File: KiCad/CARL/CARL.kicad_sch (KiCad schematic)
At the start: 46 parts, among them J1 Barrel_Jack (5V DC Supply), SW1 Beat_In_1, SW10 Power Switch, SW11 Mute_Button, SW12 Move_Left_Button, SW13 Move_Right_Button, SW14 Play_Button, SW2 Beat_In_2, SW3 Beat_In_3, SW4 Beat_In_4, SW5 Beat_In_5, SW6 Beat_In_6, SW7 Beat_In_7, SW8 Beat_In_8, SW9 Save_and_Load_Button, U1 NHD-0420H1Z (LCD), U2 MIC5365-3.3YC5 (5V to 3.3V re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, U3 MAX98357A (Amplifier), U4 TLC5947DAP (LED Driver), U5 MCP23017_SO

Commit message: PCB V2 and Schematic V3
-Updated schematic to utilize new voltage regulator setup.
-Updated PCB to reflect changes done in the schematic
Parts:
- removed U2: MIC5365-3.3YC5 (5V to 3.3V regulator), Package_TO_SOT_SMD:SOT-353_SC-70-5, symbol Regulator_Linear:MIC5365-3.3YC5
- added C10, C3, C4, C5, C6, C8, C9: 100nF, Capacitor_SMD:C_0805_2012Metric, symbol Device:C_Small
- added C7: 100nf, Capacitor_SMD:C_0805_2012Metric, symbol Device:C_Small
- added U2, U7, U9: L7805 (5V Voltage Regulator), Package_TO_SOT_THT:TO-220-3_Vertical, symbol Regulator_Linear:L7805
- added U6, U8: LD1117V33 (3.3V Voltage Regulator), Package_TO_SOT_THT:TO-220-3_Vertical, symbol Regulator_Linear:LD1117V33
- C1: value 330nF -> 100nf
- J1: value Barrel_Jack (5V DC Supply) -> Barrel_Jack (9V DC Supply)
- RV2: value Gain_Control -> Gain_Control (10k POT); footprint Potentiometer_THT:Potentiometer_Bourns_3009Y_Horizontal -> Potentiometer_SMD:Potentiometer_ACP_CA6-VSMD_Vertical
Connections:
- net GND: now also C10.2, C3.2, C4.2, C5.2, C6.2, C7.2, C8.2, C9.2, U2.2 (GND), U6.1 (GND), U7.2 (GND), U8.1 (GND), U9.2 (GND)
- net 5V -ESP32 Power: now reaches A1.26 (USB)
- net 5V -ESP32 Power: now also C4.1, U2.3 (OUT)
- net 3.3V renamed 3.3V -LCD Power
- net 3.3V -LCD Power: now also U6.2 (VO); no longer A1.2 (3V3), U5.17 (A2), U5.9 (VDD)
- net 5V renamed 5V -LED Driver Power
- net 5V -LED Driver Power: now also C10.1, U9.3 (OUT); no longer C1.1, R18.2, RV2.1, SW10.2 (B), U3.7 (VDD), U3.8 (VDD)
- new net: C1.1, C3.1, C5.1, C7.1, C9.1, SW10.2 (B), U2.1 (IN), U6.3 (VI), U7.1 (IN), U8.3 (VI), U9.1 (IN)
- new net 3.3V -GPIO Extender Power: C8.1, U5.17 (A2), U5.9 (VDD), U8.2 (VO)
- new net 5V -Amplifier Power: C6.1, R18.2, RV2.1, U3.7 (VDD), U3.8 (VDD), U7.3 (OUT)
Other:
- note added: "Power Module"
- moved on the sheet: C1, C2

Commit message: Minor Schematic Update
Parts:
- added R1, R2: 4.7Kohm, Resistor_SMD:R_0805_2012Metric, symbol Device:R_Small_US
- added R3: 0ohm, Resistor_SMD:R_0805_2012Metric, symbol Device:R_Small_US
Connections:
- net at U3.1 (DIN): now also A1.5 (DAC2/A0); no longer A1.7 (I34/A2)
- net at U3.14 (LRCLK): now also A1.11 (SCK/IO5); no longer A1.9 (IO36/A4)
- net at U3.16 (BCLK): now also A1.6 (DAC1/A1); no longer A1.8 (I39/A3)
- net at A1.10 (IO4/A5): now also U4.3 (SCLK)
- net at U1.4 (RS): now also A1.13 (MISO/IO19); no longer A1.11 (SCK/IO5)
- net at A1.14 (RX/IO16): now also R3.1; no longer U4.29 (SOUT)
- net at A1.17 (SDA/IO23), U5.13 (SDA): now also R1.2
- net at A1.18 (SCL/IO22), U5.12 (SCK): now also R2.2; no longer U4.3 (SCLK)
- new net: R3.2, U4.29 (SOUT)
- no-connect marks 23 -> 22
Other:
- note added: "Multiple of same voltage regulators to reduce heat produced by the regulators."
- note removed: "Says SCK (SPI clock) but chip uses I2C (SLC). Odd pin labeling or error on our part?"

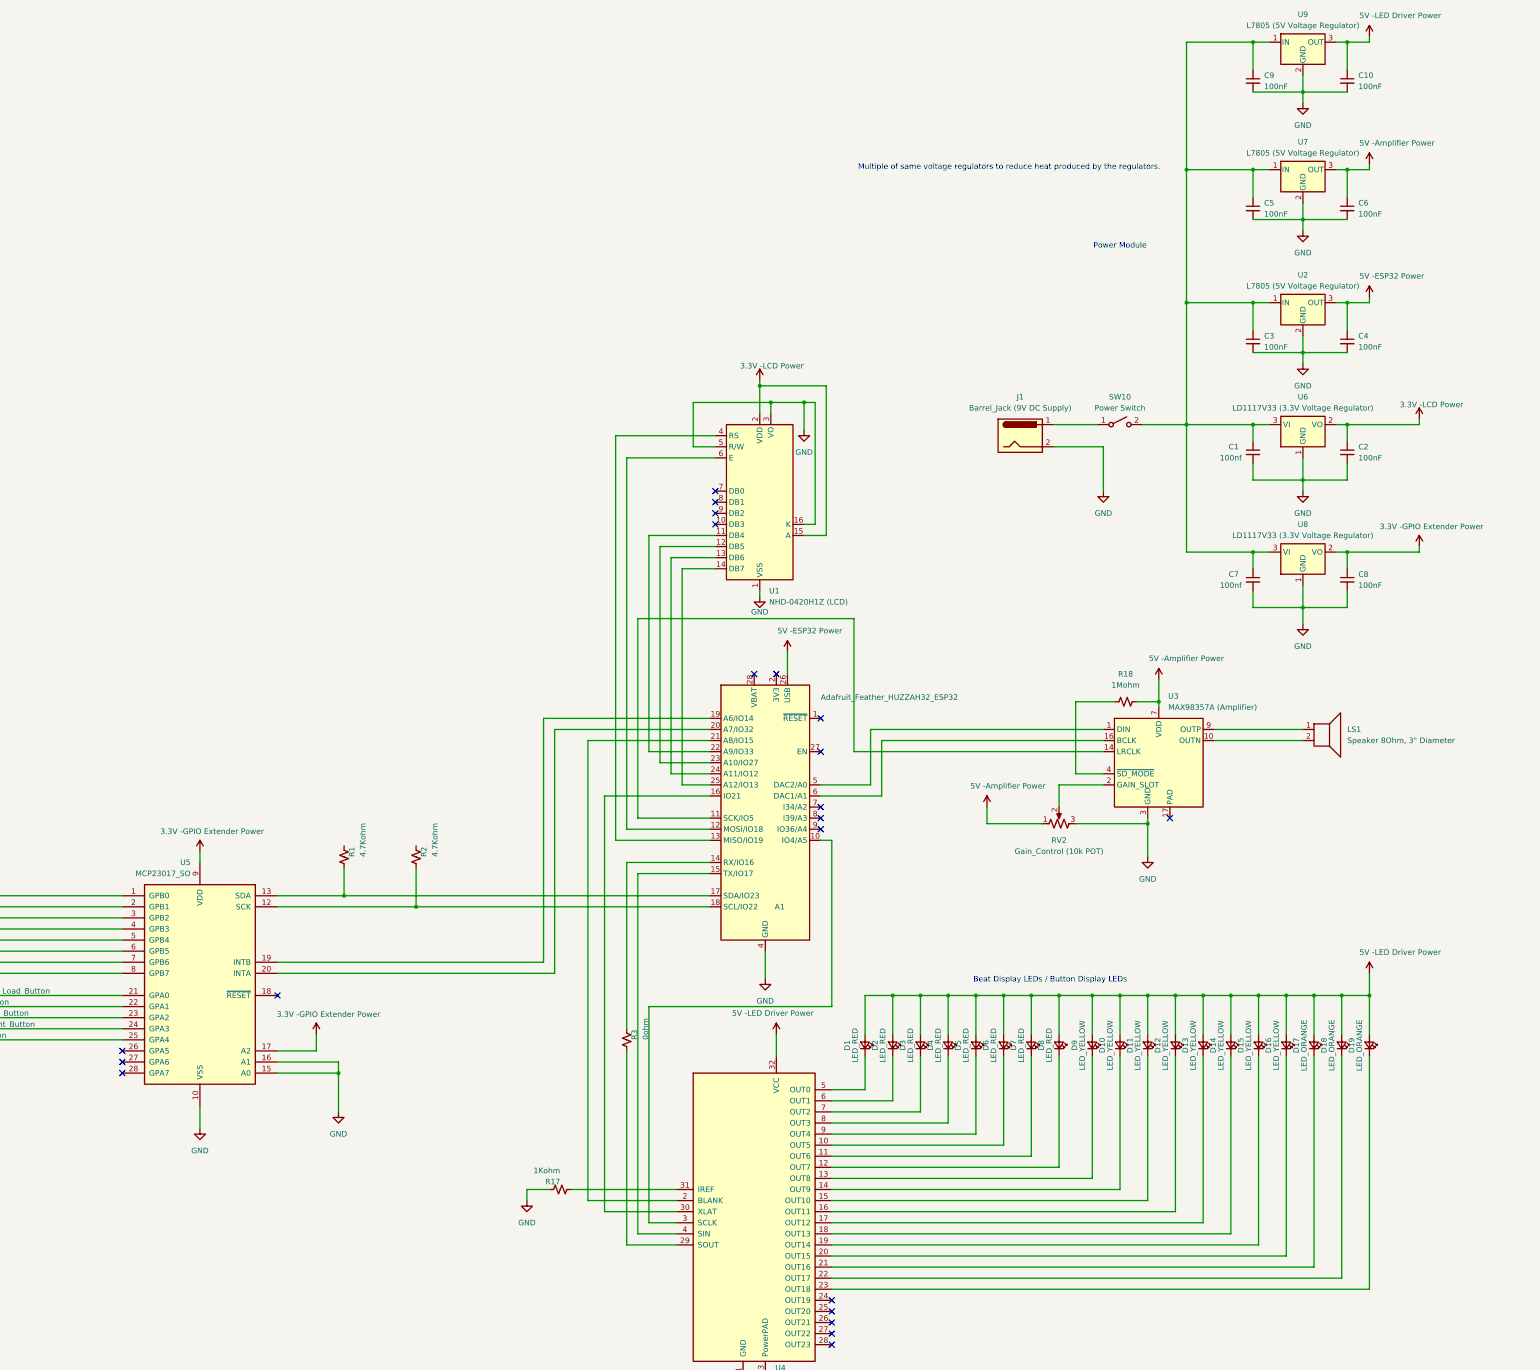
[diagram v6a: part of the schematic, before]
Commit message: Final Schematic and PCB
-Added test points  and 0 ohm resistors to the schematic.
-Added pullup resistors to I2C line
-Updated PCB and redid layout according to updated schematic.
-LED footprint updated to typical through hole PCB.
-Generated Gerbur Files
-Added Mounting Holes and Silkscreen
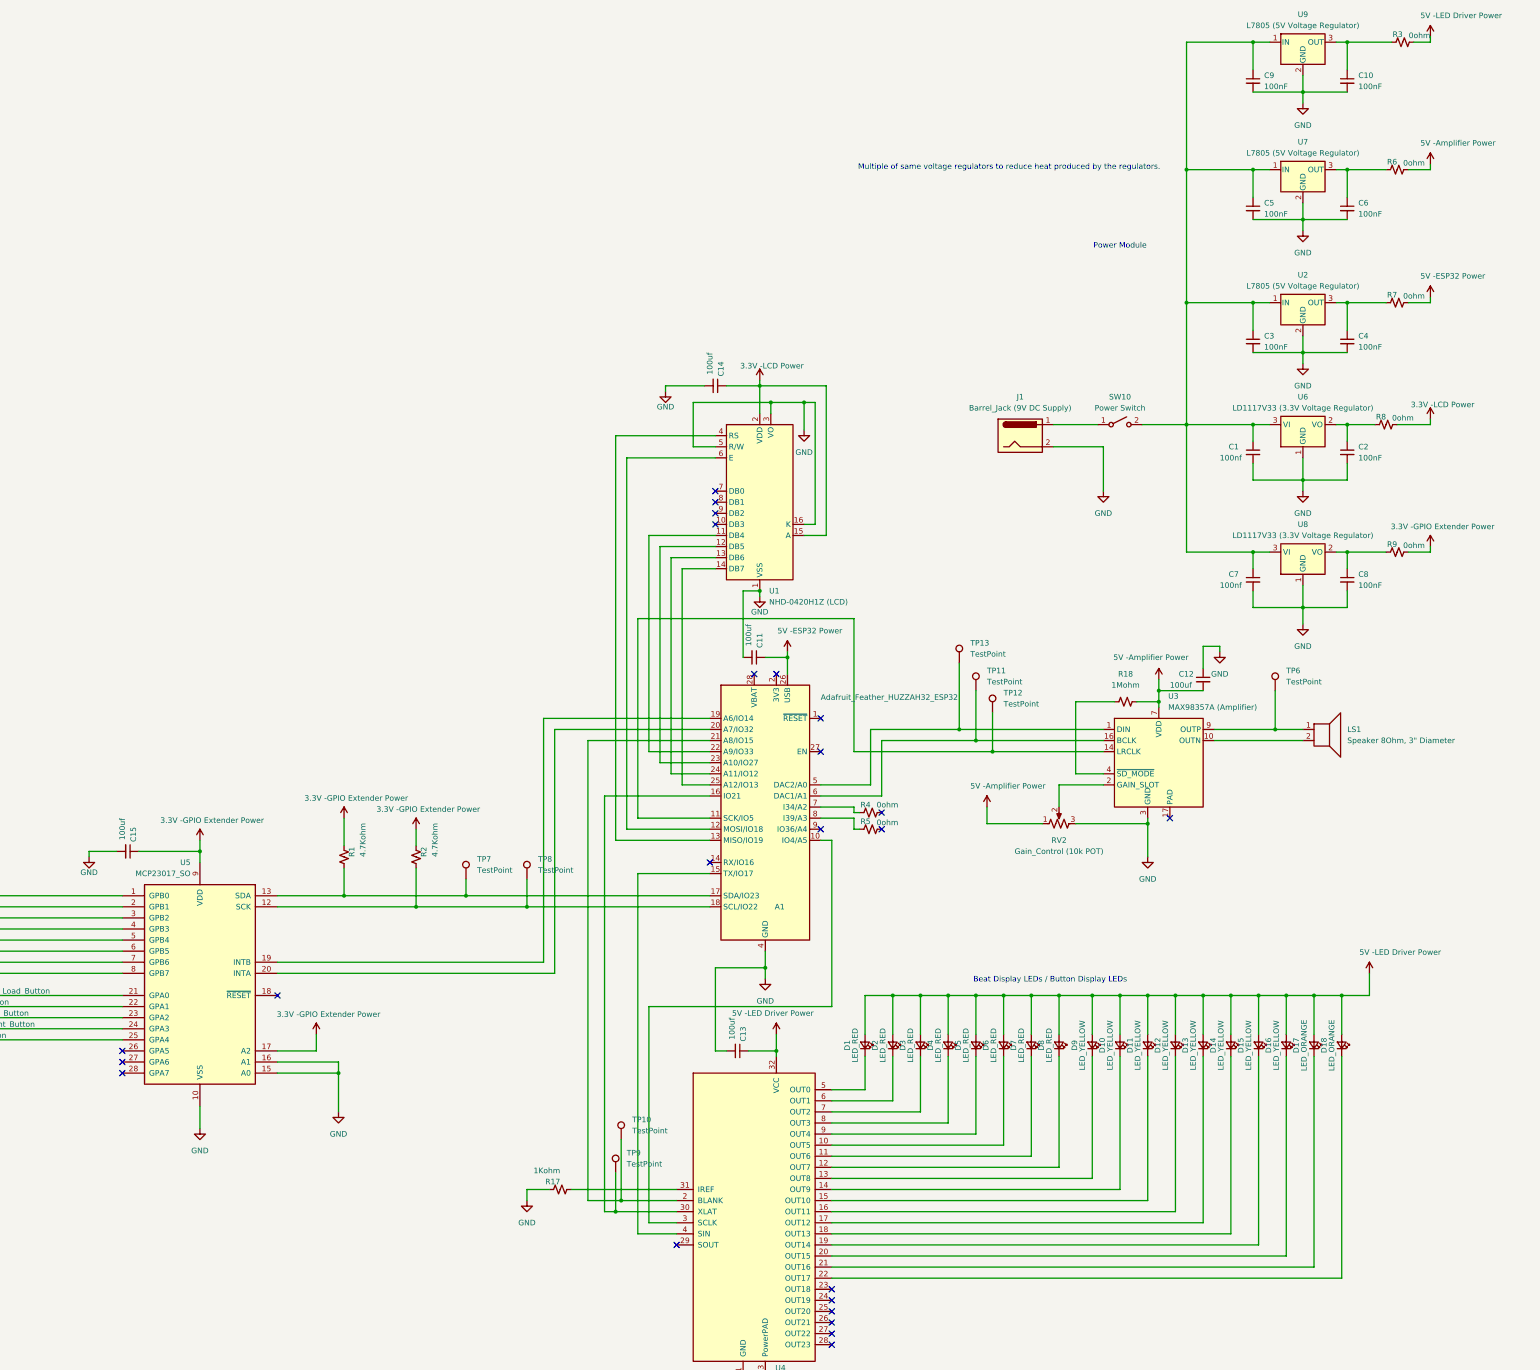
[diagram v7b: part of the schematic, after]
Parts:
- removed D19: LED_ORANGE, LED_SMD:LED_0805_2012Metric, symbol Device:LED_Small
- added C11, C12, C13, C14, C15: 100uf, Capacitor_SMD:C_0805_2012Metric, symbol Device:C_Small
- added R4, R5, R6, R7, R8, R9: 0ohm, Connector_PinHeader_2.54mm:PinHeader_1x02_P2.54mm_Vertical, symbol Device:R_Small_US
- added TP10, TP11, TP12, TP13, TP6, TP7, TP8, TP9: TestPoint, Connector_PinHeader_2.54mm:PinHeader_1x01_P2.54mm_Vertical, symbol Connector:TestPoint
- D1, D10, D11, D12, D13, D14, D15, D16, D17, D18, D2, D3, D4, D5, D6, D7, D8, D9: footprint LED_SMD:LED_0805_2012Metric -> LED_THT:LED_D5.0mm
- R3: footprint Resistor_SMD:R_0805_2012Metric -> Connector_PinHeader_2.54mm:PinHeader_1x02_P2.54mm_Vertical
- SW10: footprint Button_Switch_Keyboard:SW_Cherry_MX_1.00u_PCB -> Button_Switch_SMD:SW_DIP_SPSTx01_Slide_6.7x4.1mm_W6.73mm_P2.54mm_LowProfile_JPin
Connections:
- net 3.3V -GPIO Extender Power: now also R1.1, R2.1, C15.1, R9.2; no longer C8.1, U8.2 (VO)
- net 3.3V -LCD Power: now also C14.1, R8.2; no longer C2.1, U6.2 (VO)
- net 5V -Amplifier Power: now also C12.2, R6.2; no longer C6.1, U7.3 (OUT)
- net 5V -ESP32 Power: now also C11.1, R7.2; no longer C4.1, U2.3 (OUT)
- net 5V -LED Driver Power: now also R3.2, C13.1; no longer C10.1, U9.3 (OUT)
- net GND: now also C11.2, C12.1, C13.2, C14.2, C15.2
- net at A1.5 (DAC2/A0), U3.1 (DIN): now also TP13.1
- net at A1.11 (SCK/IO5), U3.14 (LRCLK): now also TP12.1
- net at A1.6 (DAC1/A1), U3.16 (BCLK): now also TP11.1
- net at LS1.1, U3.9 (OUTP): now also TP6.1
- net at A1.14 (RX/IO16): no longer R3.1
- net at A1.16 (IO21), U4.30 (XLAT): now also TP9.1
- net at A1.17 (SDA/IO23), R1.2, U5.13 (SDA): now also TP7.1
- net at A1.18 (SCL/IO22), R2.2, U5.12 (SCK): now also TP8.1
- net at A1.21 (A8/IO15), U4.2 (BLANK): now also TP10.1
- net at A1.7 (I34/A2): now also R4.1
- net at A1.8 (I39/A3): now also R5.1
- net at U4.29 (SOUT): no longer R3.2
- new net: C6.1, R6.1, U7.3 (OUT)
- new net: C4.1, R7.1, U2.3 (OUT)
- new net: C2.1, R8.1, U6.2 (VO)
- new net: C10.1, R3.1, U9.3 (OUT)
- new net: C8.1, R9.1, U8.2 (VO)
- no-connect marks 22 -> 25
